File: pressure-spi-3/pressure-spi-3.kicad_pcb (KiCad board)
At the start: 2 copper layers, 45 x 11 mm, 11 parts, among them J1 Conn_01x08_Male, U1 TruStability_SPI, U2 TruStability_SPI, U3 TruStability_SPI

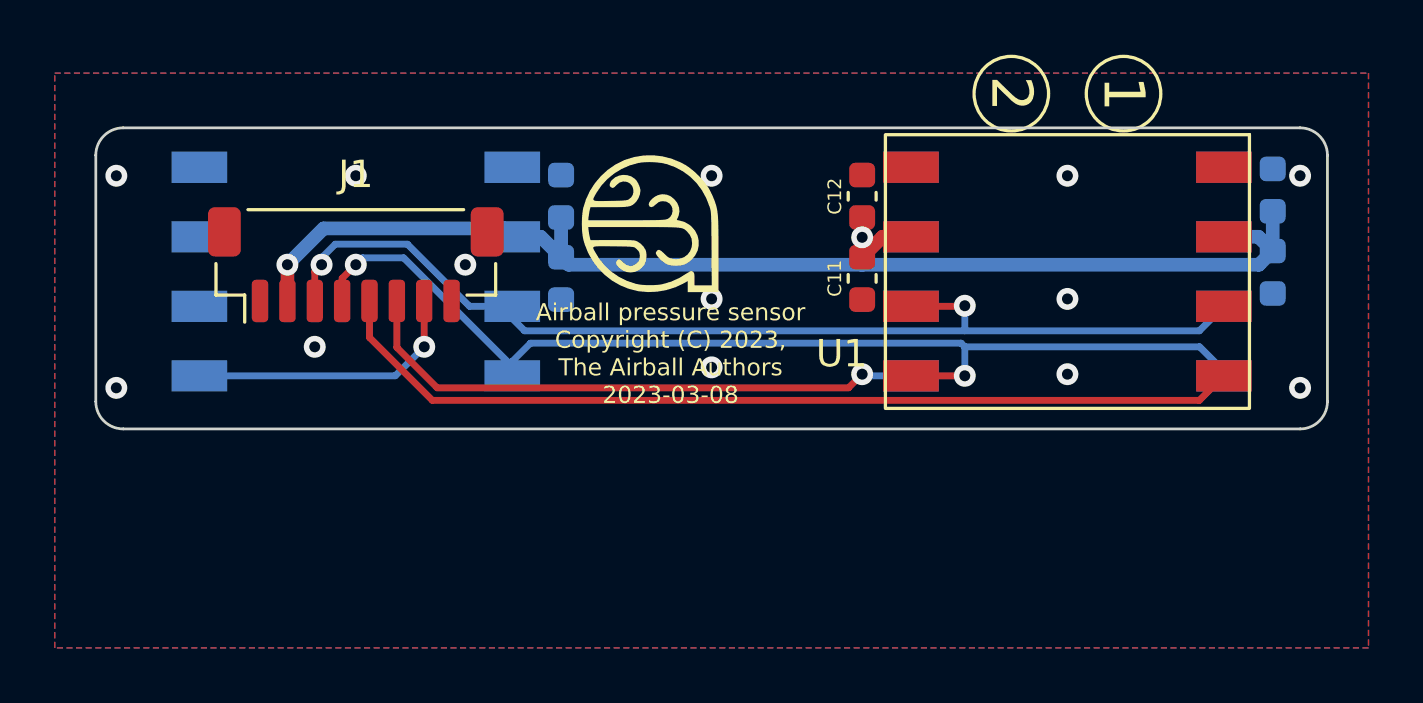
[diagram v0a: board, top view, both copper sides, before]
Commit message: Moved 8-pin connector for better clearance.
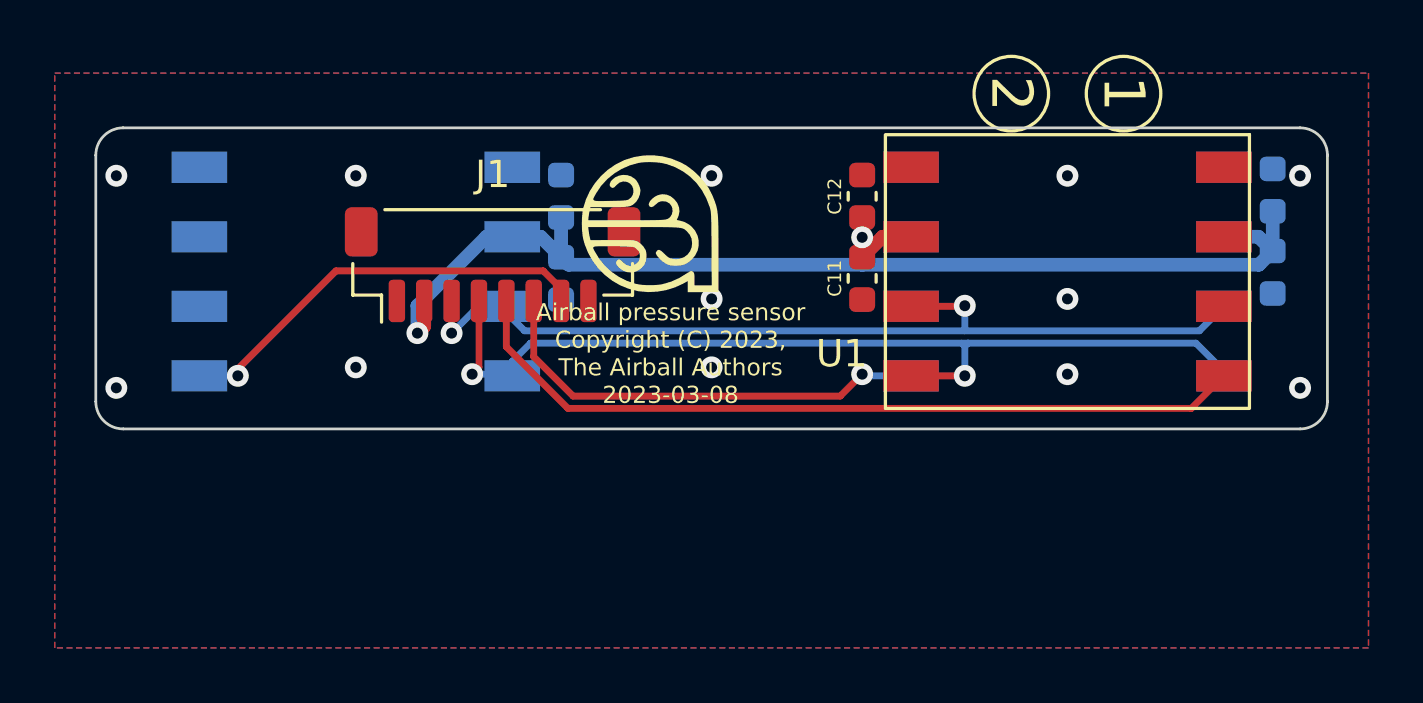
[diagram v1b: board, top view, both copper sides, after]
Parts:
- moved J1 5.00 mm to (-8.00, 5.00)
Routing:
- net /MISO: track 39.9 -> 33.9 mm
- net /!CS2: track 10.3 -> 15.7 mm
- net /SCLK: track 40.0 -> 34.9 mm
- net /!CS0: track 33.9 -> 29.3 mm
- net /!CS1: track 21.3 -> 16.8 mm
- net +3V3: track 48.1 -> 44.6 mm
- net GND: vias 13 -> 12

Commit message: Minor appearance finishing touches.
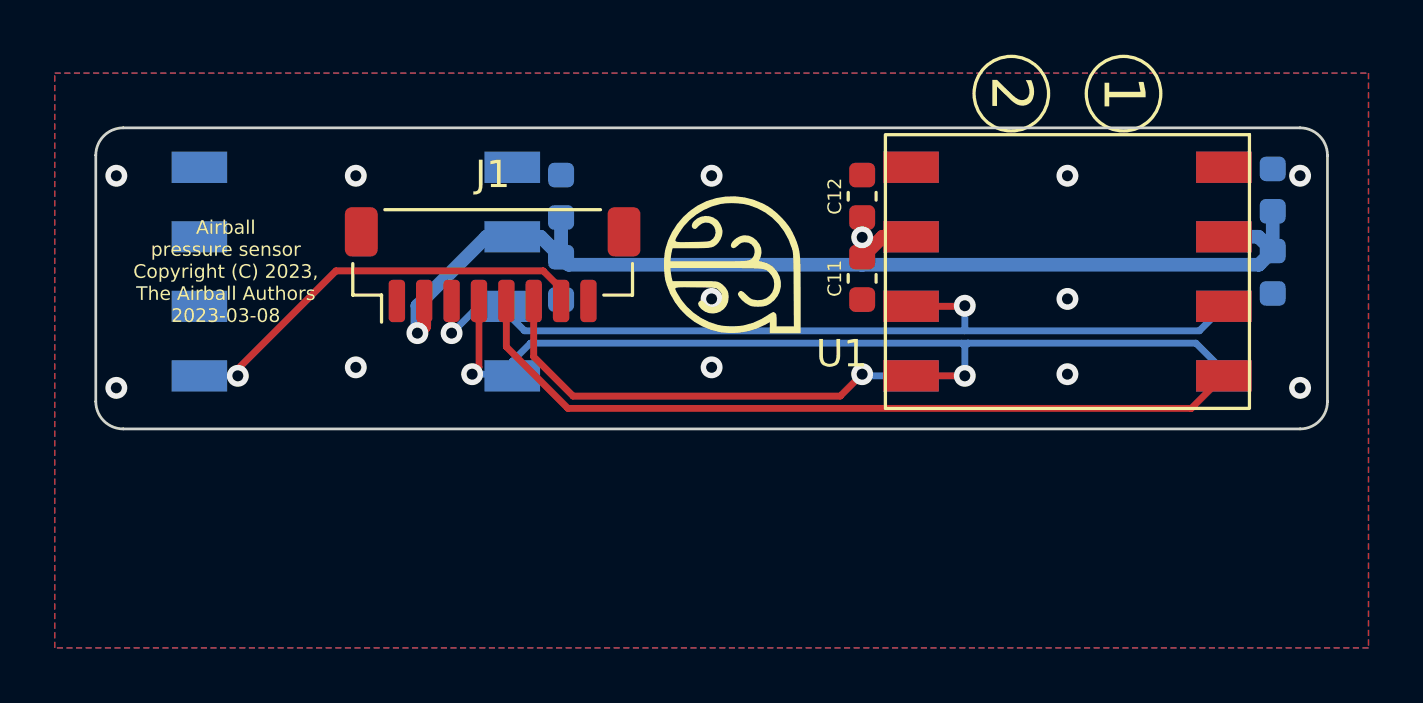
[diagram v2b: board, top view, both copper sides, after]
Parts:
- moved G*** 3.35 mm to (0.75, 5.00)
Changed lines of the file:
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@@
   )
   (footprint "airball-hardware:airball-logo-5mm" (layer "F.Cu")
-    (at -2.25 3.5)
+    (at 0.75 5)
     (attr board_only exclude_from_pos_files exclude_from_bom)
     (fp_text reference "G***" (at 0 0) (layer "F.SilkS") hide
@@
   (gr_arc (start 22.5 10) (mid 22.207107 10.707107) (end 21.5 11) (layer "Edge.Cuts") (width 0.1))
   (gr_arc (start -21.5 11) (mid -22.207107 10.707107) (end -22.5 10) (layer "Edge.Cuts") (width 0.1))
-  (gr_text "Airball pressure sensor\nCopyright (C) 2023,\nThe Airball Authors\n2023-03-08" (at -1.5 8.25) (layer "F.SilkS")
-    (effects (font (size 0.625 0.625) (thickness 0.125)))
+  (gr_text "Airball\npressure sensor\nCopyright (C) 2023,\nThe Airball Authors\n2023-03-08" (at -17.75 5.25) (layer "F.SilkS")
+    (effects (font (size 0.5 0.5) (thickness 0.125)))
   )
   (segment (start -10.5 7.25) (end -10.75 7.5) (width 0.5) (layer "F.Cu") (net 1))

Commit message: Finished design and produced fab outputs.
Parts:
- moved C11 0.25 mm to (5.25, 5.50)
- moved C12 0.25 mm to (5.25, 2.50)
- moved C21 0.25 mm to (20.8, 5.28)
- moved C22 0.25 mm to (20.8, 2.27)
- moved C31 0.25 mm to (-5.25, 5.50)
- moved C32 0.25 mm to (-5.25, 2.50)
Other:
- board text added: "Airball pressure sensor Copyright © 2023, The Airball authors 2023-03-14"
- board text removed: "Airball pressure sensor Copyright (C) 2023, The Airball Authors 2023-03-08"
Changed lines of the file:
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@@
     (pad "8" smd roundrect (at 3.5 1.325) (size 0.6 1.55) (layers "F.Cu" "F.Paste" "F.Mask") (roundrect_rratio 0.25)
       (net 3 "unconnected-(J1-Pad8)") (pinfunction "Pin_8") (pintype "passive"))
-    (pad "MP" smd roundrect (at -4.8 -1.2) (size 1.2 1.8) (layers "F.Cu" "F.Paste" "F.Mask") (roundrect_rratio 0.208333)
+    (pad "MP" smd roundrect (at -4.8 -1.2) (size 1.2 1.8) (layers "F.Cu" "F.Paste" "F.Mask") (roundrect_rratio 0.2083333333)
       (net 2 "GND"))
-    (pad "MP" smd roundrect (at 4.8 -1.2) (size 1.2 1.8) (layers "F.Cu" "F.Paste" "F.Mask") (roundrect_rratio 0.208333)
+    (pad "MP" smd roundrect (at 4.8 -1.2) (size 1.2 1.8) (layers "F.Cu" "F.Paste" "F.Mask") (roundrect_rratio 0.2083333333)
       (net 2 "GND"))
     (model "/home/ihab/airball-hardware/lib/airball-hardware.pretty/BM08B-SRSS-TB.STEP"
@@
   )
   (footprint "Capacitor_SMD:C_0603_1608Metric" (layer "F.Cu")
-    (at 5.5 5.5 -90)
+    (at 5.25 5.5 -90)
     (descr "Capacitor SMD 0603 (1608 Metric), square (rectangular) end terminal, IPC_7351 nominal, (Body size source: IPC-SM-782 page 76, https://www.pcb-3d.com/wordpress/wp-content/uploads/ipc-sm-782a_amendment_1_and_2.pdf), generated with kicad-footprint-generator")
     (tags "capacitor")
@@
   )
   (footprint "Capacitor_SMD:C_0603_1608Metric" (layer "F.Cu")
-    (at 5.5 2.5 90)
+    (at 5.25 2.5 90)
     (descr "Capacitor SMD 0603 (1608 Metric), square (rectangular) end terminal, IPC_7351 nominal, (Body size source: IPC-SM-782 page 76, https://www.pcb-3d.com/wordpress/wp-content/uploads/ipc-sm-782a_amendment_1_and_2.pdf), generated with kicad-footprint-generator")
     (tags "capacitor")
@@
   )
   (footprint "Capacitor_SMD:C_0603_1608Metric" (layer "B.Cu")
-    (at -5.5 5.5 -90)
+    (at -5.25 5.5 -90)
     (descr "Capacitor SMD 0603 (1608 Metric), square (rectangular) end terminal, IPC_7351 nominal, (Body size source: IPC-SM-782 page 76, https://www.pcb-3d.com/wordpress/wp-content/uploads/ipc-sm-782a_amendment_1_and_2.pdf), generated with kicad-footprint-generator")
     (tags "capacitor")
@@
   )
   (footprint "Capacitor_SMD:C_0603_1608Metric" (layer "B.Cu")
-    (at 20.5 5.275 -90)
+    (at 20.75 5.275 -90)
     (descr "Capacitor SMD 0603 (1608 Metric), square (rectangular) end terminal, IPC_7351 nominal, (Body size source: IPC-SM-782 page 76, https://www.pcb-3d.com/wordpress/wp-content/uploads/ipc-sm-782a_amendment_1_and_2.pdf), generated with kicad-footprint-generator")
     (tags "capacitor")
@@
   )
   (footprint "Capacitor_SMD:C_0603_1608Metric" (layer "B.Cu")
-    (at -5.5 2.5 90)
+    (at -5.25 2.5 90)
     (descr "Capacitor SMD 0603 (1608 Metric), square (rectangular) end terminal, IPC_7351 nominal, (Body size source: IPC-SM-782 page 76, https://www.pcb-3d.com/wordpress/wp-content/uploads/ipc-sm-782a_amendment_1_and_2.pdf), generated with kicad-footprint-generator")
     (tags "capacitor")
@@
   )
   (footprint "Capacitor_SMD:C_0603_1608Metric" (layer "B.Cu")
-    (at 20.5 2.275 90)
+    (at 20.75 2.275 90)
     (descr "Capacitor SMD 0603 (1608 Metric), square (rectangular) end terminal, IPC_7351 nominal, (Body size source: IPC-SM-782 page 76, https://www.pcb-3d.com/wordpress/wp-content/uploads/ipc-sm-782a_amendment_1_and_2.pdf), generated with kicad-footprint-generator")
     (tags "capacitor")
@@
   (gr_arc (start 22.5 10) (mid 22.207107 10.707107) (end 21.5 11) (layer "Edge.Cuts") (width 0.1))
   (gr_arc (start -21.5 11) (mid -22.207107 10.707107) (end -22.5 10) (layer "Edge.Cuts") (width 0.1))
-  (gr_text "Airball\npressure sensor\nCopyright (C) 2023,\nThe Airball Authors\n2023-03-08" (at -17.75 5.25) (layer "F.SilkS")
+  (gr_text "Airball\npressure sensor\nCopyright © 2023,\nThe Airball authors\n2023-03-14" (at -17.75 5.25) (layer "F.SilkS")
     (effects (font (size 0.5 0.5) (thickness 0.125)))
   )
   (segment (start -10.5 7.25) (end -10.75 7.5) (width 0.5) (layer "F.Cu") (net 1))
-  (segment (start 6.245 3.98) (end 5.5 4.725) (width 0.5) (layer "F.Cu") (net 1))
+  (segment (start 5.27 3.98) (end 7.284 3.98) (width 0.5) (layer "F.Cu") (net 1))
+  (segment (start 5.25 4) (end 5.27 3.98) (width 0.5) (layer "F.Cu") (net 1))
   (segment (start -10.5 6.325) (end -10.5 7.25) (width 0.5) (layer "F.Cu") (net 1))
-  (segment (start 7.284 3.98) (end 6.245 3.98) (width 0.5) (layer "F.Cu") (net 1))
-  (segment (start 5.5 4) (end 5.5 4.725) (width 0.5) (layer "F.Cu") (net 1))
-  (segment (start 5.5 3.275) (end 5.5 4) (width 0.5) (layer "F.Cu") (net 1))
-  (via (at 5.5 4) (size 0.8) (drill 0.4) (layers "F.Cu" "B.Cu") (net 1))
+  (segment (start 5.25 3.275) (end 5.25 4) (width 0.5) (layer "F.Cu") (net 1))
+  (segment (start 5.25 4) (end 5.25 4.725) (width 0.5) (layer "F.Cu") (net 1))
+  (via (at 5.25 4) (size 0.8) (drill 0.4) (layers "F.Cu" "B.Cu") (net 1))
   (via (at -10.75 7.5) (size 0.8) (drill 0.4) (layers "F.Cu" "B.Cu") (net 1))
-  (segment (start -5.5 4.725) (end -5.2235 5.0015) (width 0.5) (layer "B.Cu") (net 1))
-  (segment (start 20.5 3.05) (end 20.5 4.5) (width 0.5) (layer "B.Cu") (net 1))
+  (segment (start 5.25 5) (end 5.2515 5.0015) (width 0.5) (layer "B.Cu") (net 1))
   (segment (start -8.23 3.98) (end -7.284 3.98) (width 0.5) (layer "B.Cu") (net 1))
-  (segment (start -6.245 3.98) (end -5.5 4.725) (width 0.5) (layer "B.Cu") (net 1))
-  (segment (start -7.284 3.98) (end -6.245 3.98) (width 0.5) (layer "B.Cu") (net 1))
+  (segment (start 18.716 3.98) (end 20.23 3.98) (width 0.5) (layer "B.Cu") (net 1))
+  (segment (start 20.2485 5.0015) (end 20.75 4.5) (width 0.5) (layer "B.Cu") (net 1))
+  (segment (start -5.995 3.98) (end -4.9735 5.0015) (width 0.5) (layer "B.Cu") (net 1))
   (segment (start -10.75 7.5) (end -10.75 6.5) (width 0.5) (layer "B.Cu") (net 1))
-  (segment (start 19.9985 5.0015) (end 20.5 4.5) (width 0.5) (layer "B.Cu") (net 1))
-  (segment (start 19.98 3.98) (end 20.5 4.5) (width 0.5) (layer "B.Cu") (net 1))
-  (segment (start 5.4985 5.0015) (end 19.9985 5.0015) (width 0.5) (layer "B.Cu") (net 1))
   (segment (start -10.75 6.5) (end -8.23 3.98) (width 0.5) (layer "B.Cu") (net 1))
-  (segment (start 18.716 3.98) (end 19.98 3.98) (width 0.5) (layer "B.Cu") (net 1))
-  (segment (start -5.2235 5.0015) (end 5.4985 5.0015) (width 0.5) (layer "B.Cu") (net 1))
-  (segment (start 5.5 5) (end 5.4985 5.0015) (width 0.5) (layer "B.Cu") (net 1))
-  (segment (start -5.5 3.275) (end -5.5 4.725) (width 0.5) (layer "B.Cu") (net 1))
-  (segment (start 5.5 4) (end 5.5 5) (width 0.5) (layer "B.Cu") (net 1))
+  (segment (start -5.25 3.275) (end -5.25 4.725) (width 0.5) (layer "B.Cu") (net 1))
+  (segment (start 5.25 4) (end 5.25 5) (width 0.5) (layer "B.Cu") (net 1))
+  (segment (start 20.75 4.5) (end 20.75 3.05) (width 0.5) (layer "B.Cu") (net 1))
+  (segment (start 20.23 3.98) (end 20.75 4.5) (width 0.5) (layer "B.Cu") (net 1))
+  (segment (start -4.9735 5.0015) (end 20.2485 5.0015) (width 0.5) (layer "B.Cu") (net 1))
+  (segment (start -7.284 3.98) (end -5.995 3.98) (width 0.5) (layer "B.Cu") (net 1))
   (via (at -13 8.75) (size 0.8) (drill 0.4) (layers "F.Cu" "B.Cu") (free) (net 2))
   (via (at -13 1.75) (size 0.8) (drill 0.4) (layers "F.Cu" "B.Cu") (free) (net 2))
